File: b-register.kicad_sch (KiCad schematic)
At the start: 12 parts

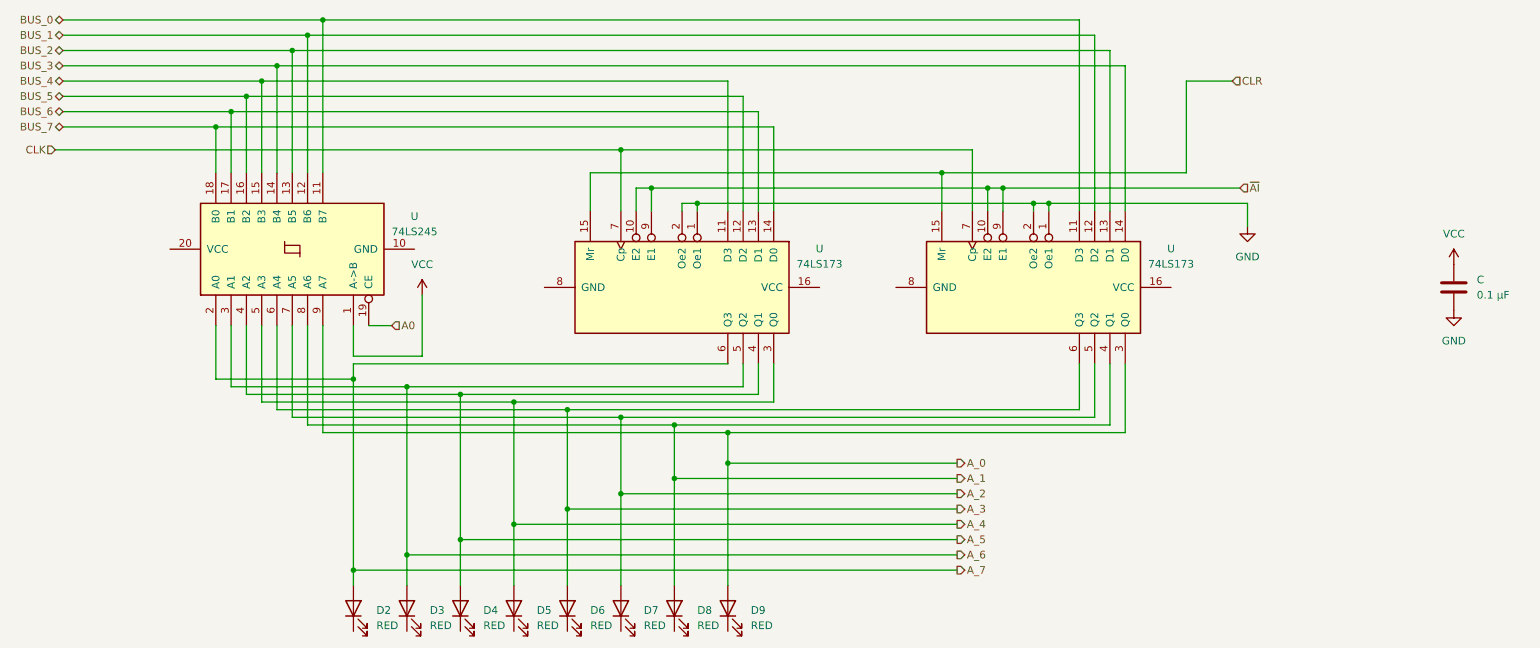
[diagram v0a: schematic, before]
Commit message: Made the a-register and edited it to make it work for the b-register
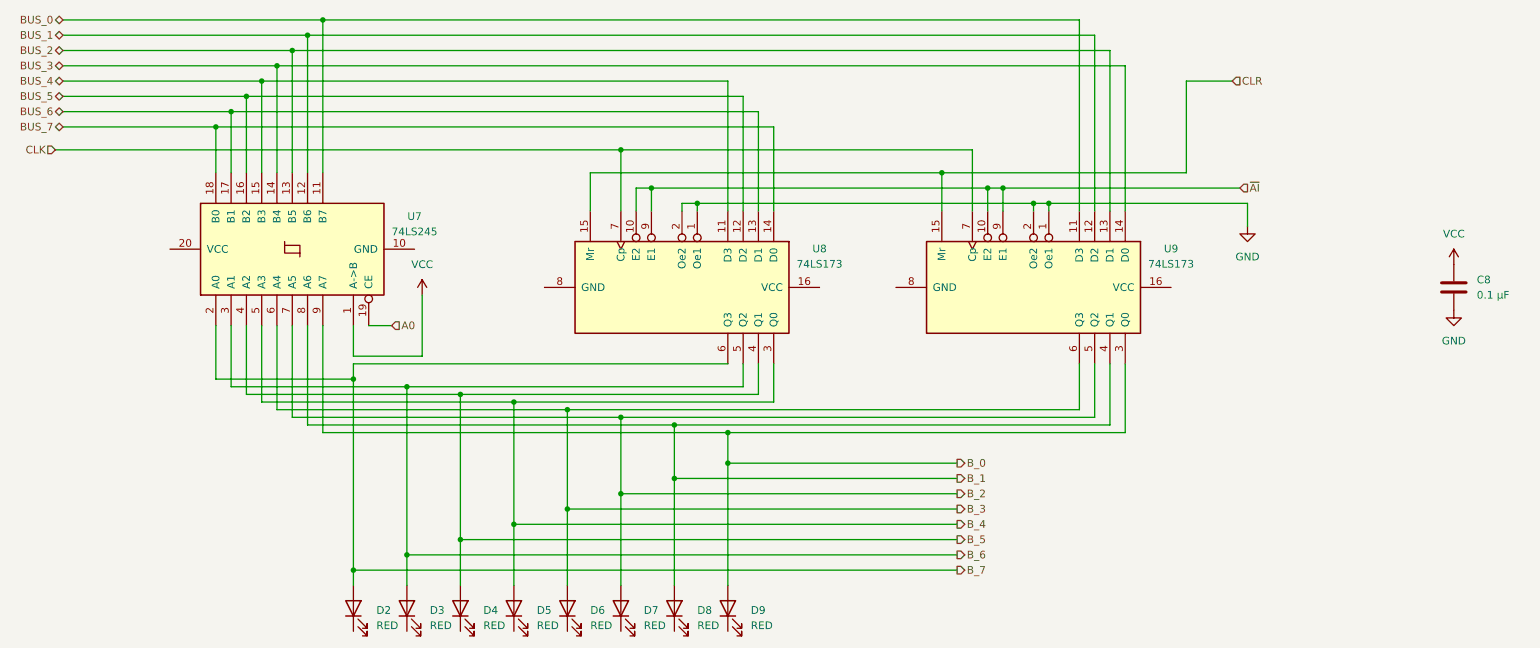
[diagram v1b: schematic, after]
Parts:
- renumbered C to C8, U to U7, U to U8, U to U9
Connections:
- net A_0 renamed B_0
- net A_1 renamed B_1
- net A_2 renamed B_2
- net A_3 renamed B_3
- net A_4 renamed B_4
- net A_5 renamed B_5
- net A_6 renamed B_6
- net A_7 renamed B_7
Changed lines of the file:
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@@
 		)
 	)
-	(hierarchical_label "A_2"
+	(hierarchical_label "B_2"
 		(shape output)
 		(at 177.8 99.06 0)
@@
 		)
 	)
-	(hierarchical_label "A_7"
+	(hierarchical_label "B_7"
 		(shape output)
 		(at 177.8 111.76 0)
@@
 		)
 	)
-	(hierarchical_label "A_3"
+	(hierarchical_label "B_3"
 		(shape output)
 		(at 177.8 101.6 0)
@@
 		)
 	)
-	(hierarchical_label "A_0"
+	(hierarchical_label "B_0"
 		(shape output)
 		(at 177.8 93.98 0)
@@
 		)
 	)
-	(hierarchical_label "A_6"
+	(hierarchical_label "B_6"
 		(shape output)
 		(at 177.8 109.22 0)
@@
 		)
 	)
-	(hierarchical_label "A_5"
+	(hierarchical_label "B_5"
 		(shape output)
 		(at 177.8 106.68 0)
@@
 		)
 	)
-	(hierarchical_label "A_1"
+	(hierarchical_label "B_1"
 		(shape output)
 		(at 177.8 96.52 0)
@@
 		)
 	)
-	(hierarchical_label "A_4"
+	(hierarchical_label "B_4"
 		(shape output)
 		(at 177.8 104.14 0)
@@
 			(project "8-Bit-PC"
 				(path "/48633dea-2de9-4b6f-aeff-2ee54233f918/01639e59-f640-4704-bff8-92b5a7e3f002"
-					(reference "D16")
+					(reference "D8")
 					(unit 1)
 				)
@@
 			(project "8-Bit-PC"
 				(path "/48633dea-2de9-4b6f-aeff-2ee54233f918/01639e59-f640-4704-bff8-92b5a7e3f002"
-					(reference "D15")
+					(reference "D7")
 					(unit 1)
 				)
@@
 		(dnp no)
 		(fields_autoplaced yes)
-		(property "Reference" "U"
+		(property "Reference" "U9"
 			(at 213.36 58.3498 90)
 			(effects
@@
 		)
 		(instances
-			(project "8-Bit-PC"
-				(path "/48633dea-2de9-4b6f-aeff-2ee54233f918/01639e59-f640-4704-bff8-92b5a7e3f002"
-					(reference "U12")
+			(project ""
+				(path "/48633dea-2de9-4b6f-aeff-2ee54233f918/01639e59-f640-4704-bff8-92b5a7e3f002"
+					(reference "U9")
+					(unit 1)
+				)
+				(path "/48633dea-2de9-4b6f-aeff-2ee54233f918/0da64945-ad09-4cb6-87e6-9538c18b83c8"
+					(reference "U9")
 					(unit 1)
 				)
@@
 		(dnp no)
 		(fields_autoplaced yes)
-		(property "Reference" "#PWR"
+		(property "Reference" "#PWR013"
 			(at 260.35 74.93 0)
 			(effects
@@
 		)
 		(instances
-			(project "8-Bit-PC"
-				(path "/48633dea-2de9-4b6f-aeff-2ee54233f918/01639e59-f640-4704-bff8-92b5a7e3f002"
-					(reference "#PWR017")
+			(project ""
+				(path "/48633dea-2de9-4b6f-aeff-2ee54233f918/01639e59-f640-4704-bff8-92b5a7e3f002"
+					(reference "#PWR013")
+					(unit 1)
+				)
+				(path "/48633dea-2de9-4b6f-aeff-2ee54233f918/0da64945-ad09-4cb6-87e6-9538c18b83c8"
+					(reference "#PWR013")
 					(unit 1)
 				)
@@
 		(dnp no)
 		(fields_autoplaced yes)
-		(property "Reference" "U"
+		(property "Reference" "U7"
 			(at 87.63 52.9746 90)
 			(effects
@@
 		)
 		(instances
-			(project "8-Bit-PC"
-				(path "/48633dea-2de9-4b6f-aeff-2ee54233f918/01639e59-f640-4704-bff8-92b5a7e3f002"
-					(reference "U10")
+			(project ""
+				(path "/48633dea-2de9-4b6f-aeff-2ee54233f918/01639e59-f640-4704-bff8-92b5a7e3f002"
+					(reference "U7")
+					(unit 1)
+				)
+				(path "/48633dea-2de9-4b6f-aeff-2ee54233f918/0da64945-ad09-4cb6-87e6-9538c18b83c8"
+					(reference "U7")
 					(unit 1)
 				)
@@
 		(dnp no)
 		(fields_autoplaced yes)
-		(property "Reference" "#PWR"
+		(property "Reference" "#PWR010"
 			(at 226.06 60.96 0)
 			(effects
@@
 		)
 		(instances
-			(project "8-Bit-PC"
-				(path "/48633dea-2de9-4b6f-aeff-2ee54233f918/01639e59-f640-4704-bff8-92b5a7e3f002"
-					(reference "#PWR015")
+			(project ""
+				(path "/48633dea-2de9-4b6f-aeff-2ee54233f918/01639e59-f640-4704-bff8-92b5a7e3f002"
+					(reference "#PWR010")
+					(unit 1)
+				)
+				(path "/48633dea-2de9-4b6f-aeff-2ee54233f918/0da64945-ad09-4cb6-87e6-9538c18b83c8"
+					(reference "#PWR010")
 					(unit 1)
 				)
@@
 		(dnp no)
 		(fields_autoplaced yes)
-		(property "Reference" "#PWR"
+		(property "Reference" "#PWR012"
 			(at 260.35 64.77 0)
 			(effects
@@
 		)
 		(instances
-			(project "8-Bit-PC"
-				(path "/48633dea-2de9-4b6f-aeff-2ee54233f918/01639e59-f640-4704-bff8-92b5a7e3f002"
-					(reference "#PWR016")
+			(project ""
+				(path "/48633dea-2de9-4b6f-aeff-2ee54233f918/01639e59-f640-4704-bff8-92b5a7e3f002"
+					(reference "#PWR012")
+					(unit 1)
+				)
+				(path "/48633dea-2de9-4b6f-aeff-2ee54233f918/0da64945-ad09-4cb6-87e6-9538c18b83c8"
+					(reference "#PWR012")
 					(unit 1)
 				)
@@
 			(project "8-Bit-PC"
 				(path "/48633dea-2de9-4b6f-aeff-2ee54233f918/01639e59-f640-4704-bff8-92b5a7e3f002"
-					(reference "D10")
+					(reference "D2")
 					(unit 1)
 				)
@@
 		(dnp no)
 		(fields_autoplaced yes)
-		(property "Reference" "C"
+		(property "Reference" "C8"
 			(at 264.16 63.4999 0)
 			(effects
@@
 		)
 		(instances
-			(project "8-Bit-PC"
-				(path "/48633dea-2de9-4b6f-aeff-2ee54233f918/01639e59-f640-4704-bff8-92b5a7e3f002"
-					(reference "C9")
+			(project ""
+				(path "/48633dea-2de9-4b6f-aeff-2ee54233f918/01639e59-f640-4704-bff8-92b5a7e3f002"
+					(reference "C8")
+					(unit 1)
+				)
+				(path "/48633dea-2de9-4b6f-aeff-2ee54233f918/0da64945-ad09-4cb6-87e6-9538c18b83c8"
+					(reference "C8")
 					(unit 1)
 				)
@@
 			(project "8-Bit-PC"
 				(path "/48633dea-2de9-4b6f-aeff-2ee54233f918/01639e59-f640-4704-bff8-92b5a7e3f002"
-					(reference "D11")
+					(reference "D3")
 					(unit 1)
 				)
@@
 		(dnp no)
 		(fields_autoplaced yes)
-		(property "Reference" "#PWR"
+		(property "Reference" "#PWR011"
 			(at 88.9 69.85 0)
 			(effects
@@
 		)
 		(instances
-			(project "8-Bit-PC"
-				(path "/48633dea-2de9-4b6f-aeff-2ee54233f918/01639e59-f640-4704-bff8-92b5a7e3f002"
-					(reference "#PWR014")
+			(project ""
+				(path "/48633dea-2de9-4b6f-aeff-2ee54233f918/01639e59-f640-4704-bff8-92b5a7e3f002"
+					(reference "#PWR011")
+					(unit 1)
+				)
+				(path "/48633dea-2de9-4b6f-aeff-2ee54233f918/0da64945-ad09-4cb6-87e6-9538c18b83c8"
+					(reference "#PWR011")
 					(unit 1)
 				)
@@
 			(project "8-Bit-PC"
 				(path "/48633dea-2de9-4b6f-aeff-2ee54233f918/01639e59-f640-4704-bff8-92b5a7e3f002"
-					(reference "D12")
+					(reference "D4")
 					(unit 1)
 				)
@@
 		(dnp no)
 		(fields_autoplaced yes)
-		(property "Reference" "U"
+		(property "Reference" "U8"
 			(at 154.94 58.3498 90)
 			(effects
@@
 		)
 		(instances
-			(project "8-Bit-PC"
-				(path "/48633dea-2de9-4b6f-aeff-2ee54233f918/01639e59-f640-4704-bff8-92b5a7e3f002"
-					(reference "U11")
+			(project ""
+				(path "/48633dea-2de9-4b6f-aeff-2ee54233f918/01639e59-f640-4704-bff8-92b5a7e3f002"
+					(reference "U8")
+					(unit 1)
+				)
+				(path "/48633dea-2de9-4b6f-aeff-2ee54233f918/0da64945-ad09-4cb6-87e6-9538c18b83c8"
+					(reference "U8")
 					(unit 1)
 				)
@@
 			(project "8-Bit-PC"
 				(path "/48633dea-2de9-4b6f-aeff-2ee54233f918/01639e59-f640-4704-bff8-92b5a7e3f002"
-					(reference "D13")
+					(reference "D5")
 					(unit 1)
 				)
@@
 			(project "8-Bit-PC"
 				(path "/48633dea-2de9-4b6f-aeff-2ee54233f918/01639e59-f640-4704-bff8-92b5a7e3f002"
-					(reference "D17")
+					(reference "D9")
 					(unit 1)
 				)
@@
 			(project "8-Bit-PC"
 				(path "/48633dea-2de9-4b6f-aeff-2ee54233f918/01639e59-f640-4704-bff8-92b5a7e3f002"
-					(reference "D14")
-					(unit 1)
-				)
+					(reference "D6")
+					(unit 1)
+				)

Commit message: Added the ALU and flags register schematic.
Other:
- title: (none) -> 8 bit PC
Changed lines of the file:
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@@
 	(generator_version "9.0")
 	(paper "A4")
+	(title_block
+		(title "8 bit PC")
+		(date "2025-10-14")
+		(rev "1")
+	)
 	(junction
 		(at 57.15 35.56)
@@
 					(unit 1)
 				)
-				(path "/48633dea-2de9-4b6f-aeff-2ee54233f918/0da64945-ad09-4cb6-87e6-9538c18b83c8"
-					(reference "D8")
-					(unit 1)
-				)
 			)
 		)
@@
 					(unit 1)
 				)
-				(path "/48633dea-2de9-4b6f-aeff-2ee54233f918/0da64945-ad09-4cb6-87e6-9538c18b83c8"
-					(reference "D7")
-					(unit 1)
-				)
 			)
 		)
@@
 					(unit 1)
 				)
-				(path "/48633dea-2de9-4b6f-aeff-2ee54233f918/0da64945-ad09-4cb6-87e6-9538c18b83c8"
-					(reference "D2")
-					(unit 1)
-				)
 			)
 		)
@@
 					(unit 1)
 				)
-				(path "/48633dea-2de9-4b6f-aeff-2ee54233f918/0da64945-ad09-4cb6-87e6-9538c18b83c8"
-					(reference "D3")
-					(unit 1)
-				)
 			)
 		)
@@
 					(unit 1)
 				)
-				(path "/48633dea-2de9-4b6f-aeff-2ee54233f918/0da64945-ad09-4cb6-87e6-9538c18b83c8"
-					(reference "D4")
-					(unit 1)
-				)
 			)
 		)
@@
 					(unit 1)
 				)
-				(path "/48633dea-2de9-4b6f-aeff-2ee54233f918/0da64945-ad09-4cb6-87e6-9538c18b83c8"
-					(reference "D5")
-					(unit 1)
-				)
 			)
 		)
@@
 					(unit 1)
 				)
-				(path "/48633dea-2de9-4b6f-aeff-2ee54233f918/0da64945-ad09-4cb6-87e6-9538c18b83c8"
-					(reference "D9")
-					(unit 1)
-				)
 			)
 		)
@@
 					(reference "D6")
 					(unit 1)
-				)
-				(path "/48633dea-2de9-4b6f-aeff-2ee54233f918/0da64945-ad09-4cb6-87e6-9538c18b83c8"
-					(reference "D6")
-					(unit 1)
